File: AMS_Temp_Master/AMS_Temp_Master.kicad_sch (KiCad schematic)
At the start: 9 parts, among them J1 Conn_01x06_Pin, J2 Conn_01x02_Pin, J3 Conn_01x04_Pin, J4 Conn_01x04_Pin, U1 ATmega328P-A, U2 MCP2515-xSO, U3 MCP2551-I-SN, U4 LD1117S50TR_SOT223, Y1 CSTCE16M0V53-R0

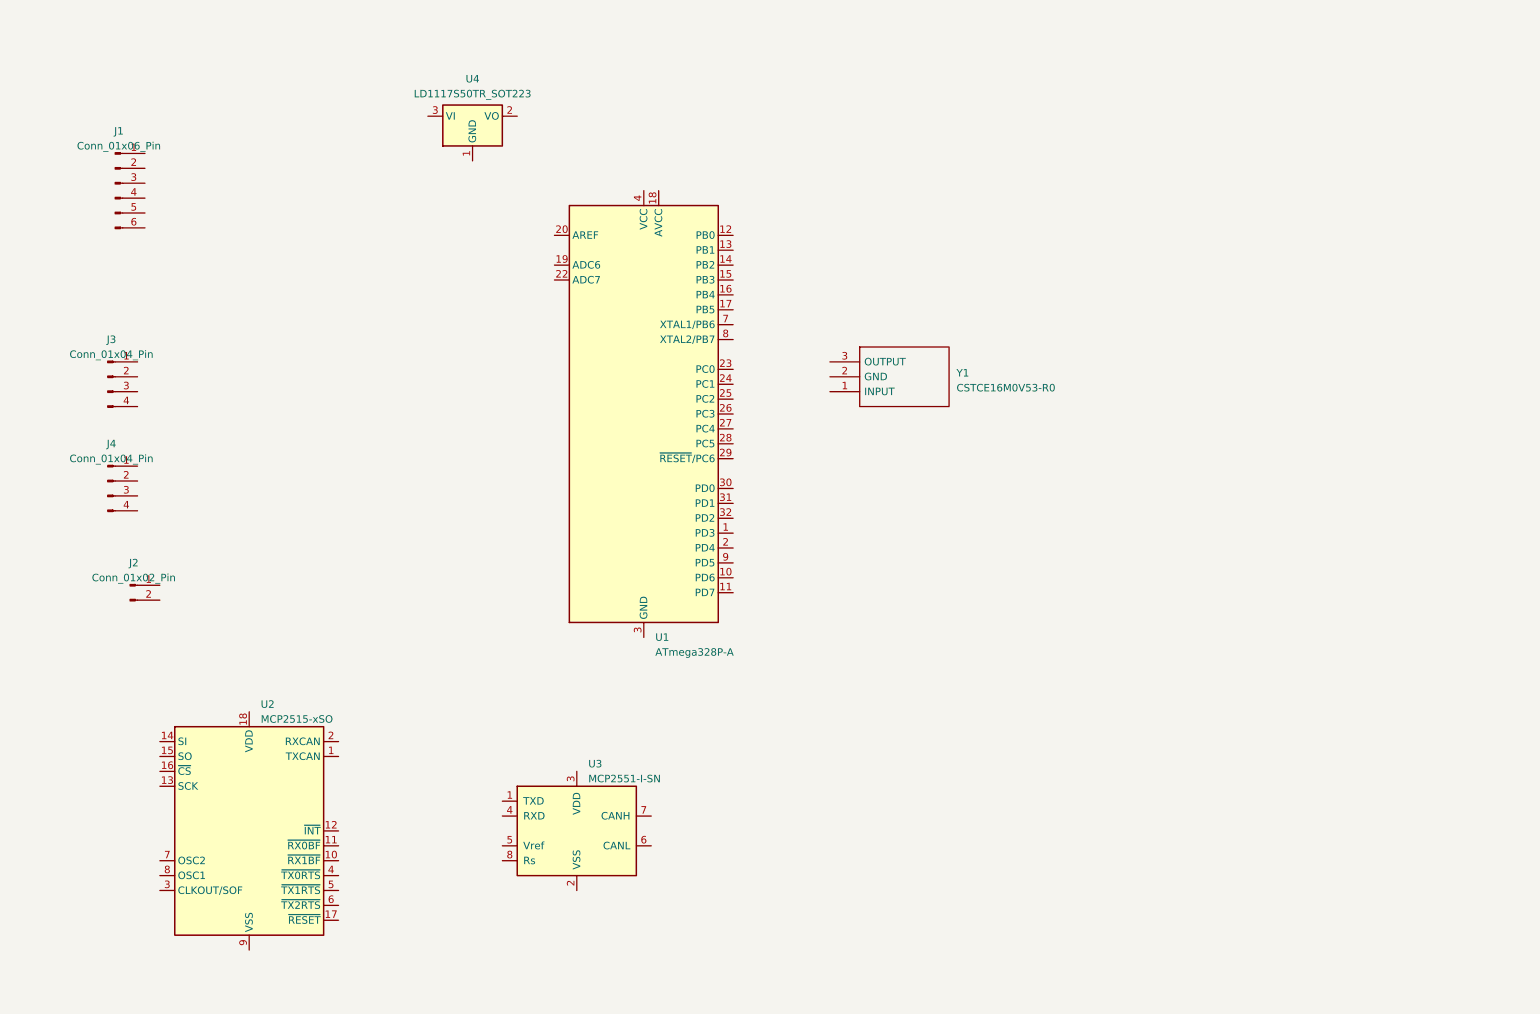
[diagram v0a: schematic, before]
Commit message: Complete AMS_Temp_Master Circuit Schematics and modify
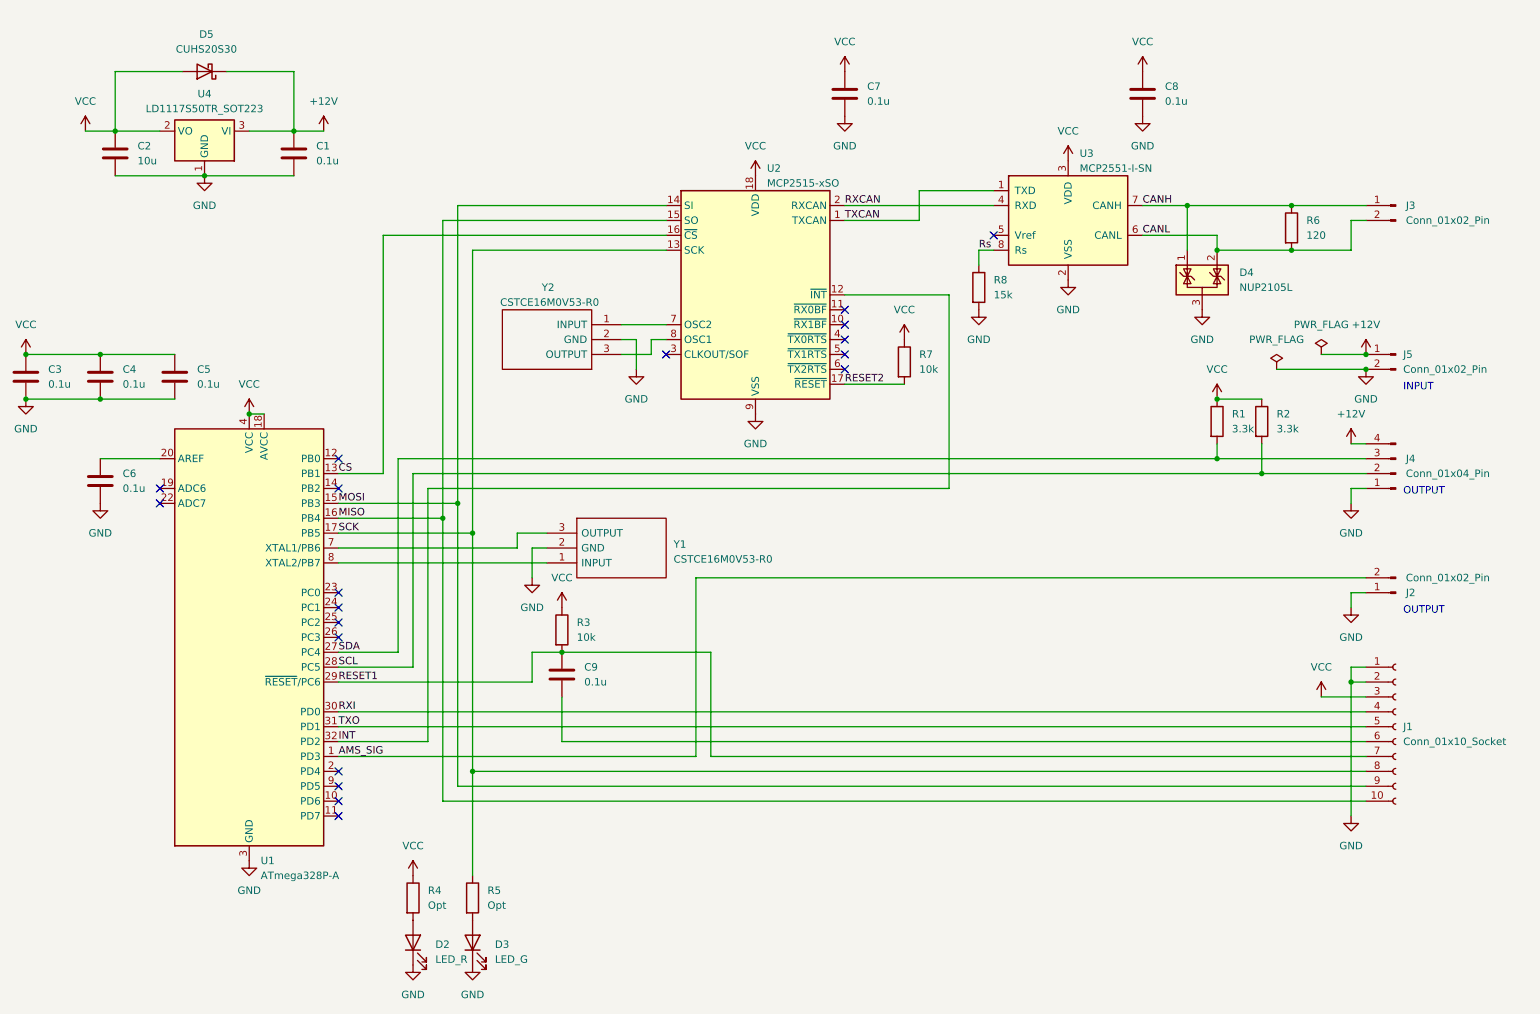
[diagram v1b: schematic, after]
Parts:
- removed J1: Conn_01x06_Pin, symbol Connector:Conn_01x06_Pin
- removed J3: Conn_01x04_Pin, symbol Connector:Conn_01x04_Pin
- added C1, C3, C4, C5, C6, C7, C8, C9: 0.1u, Capacitor_SMD:C_0603_1608Metric, symbol Device:C
- added C2: 10u, Capacitor_SMD:C_0603_1608Metric, symbol Device:C
- added D2: LED_R, LED_SMD:LED_0603_1608Metric, symbol Device:LED
- added D3: LED_G, LED_SMD:LED_0603_1608Metric, symbol Device:LED
- added D4: NUP2105L, Package_TO_SOT_SMD:SOT-23, symbol Power_Protection:NUP2105L
- added D5: CUHS20S30, SamacSys_Parts:CUHS20S40H3F, symbol Device:D_Schottky
- added J1: Conn_01x10_Socket, Connector_PinSocket_2.54mm:PinSocket_1x10_P2.54mm_Vertical, symbol Connector:Conn_01x10_Socket
- added J3, J5: Conn_01x02_Pin, Connector_JST:JST_XH_S2B-XH-A_1x02_P2.50mm_Horizontal, symbol Connector:Conn_01x02_Pin
- added R1, R2: 3.3k, Resistor_SMD:R_0603_1608Metric, symbol Device:R
- added R3, R7: 10k, Resistor_SMD:R_0603_1608Metric, symbol Device:R
- added R4, R5: Opt, Resistor_SMD:R_0603_1608Metric, symbol Device:R
- added R6: 120, Resistor_SMD:R_0603_1608Metric, symbol Device:R
- added R8: 15k, Resistor_SMD:R_0603_1608Metric, symbol Device:R
- added Y2: CSTCE16M0V53-R0, CSTCE16M0V53R0, symbol SamacSys_Parts:CSTCE16M0V53-R0
- J2: footprint (none) -> Connector_JST:JST_XH_S2B-XH-A_1x02_P2.50mm_Horizontal
- J4: footprint (none) -> Connector_JST:JST_XH_S4B-XH-A_1x04_P2.50mm_Horizontal
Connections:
- net AMS_SIG: now reaches U1.1 (PD3)
- net AMS_SIG: now also J2.2 (Pin_2)
- net CS: now reaches U1.13 (PB1)
- net CS: now also U2.16 (~{CS})
- net MOSI: now reaches U1.15 (PB3)
- net MOSI: now also U2.14 (SI), J1.9 (Pin_9)
- net MISO: now reaches U1.16 (PB4)
- net MISO: now also U2.15 (SO), J1.10 (Pin_10)
- net SCK: now reaches U1.17 (PB5)
- net SCK: now also U2.13 (SCK), J1.8 (Pin_8), R5.1
- net VCC: now reaches U1.18 (AVCC)
- net VCC: now also U1.4 (VCC), U1.6 (VCC), U2.18 (VDD), U3.3 (VDD), U4.2 (VO), C2.1, C3.1, C4.1, C5.1, C7.1, C8.1, D5.2 (A), J1.3 (Pin_3), R1.1, R2.1, R3.1, R4.1, R7.1
- net at U1.20 (AREF): now also C6.1
- net GND: now reaches U1.21 (GND), U1.3 (GND), U1.5 (GND)
- net GND: now also J2.1 (Pin_1), J4.1 (Pin_1), U2.9 (VSS), U3.2 (VSS), U4.1 (GND), Y1.2 (GND), C1.2, C2.2, C3.2, C4.2, C5.2, C6.2, C7.2, C8.2, D2.1 (K), D3.1 (K), D4.3 (A), J1.1 (Pin_1), J1.2 (Pin_2), J5.2 (Pin_2), R8.2, Y2.2 (GND)
- net SDA: now reaches U1.27 (PC4)
- net SDA: now also J4.3 (Pin_3), R1.2
- net SCL: now reaches U1.28 (PC5)
- net SCL: now also J4.2 (Pin_2), R2.2
- net RESET1: now reaches U1.29 (~{RESET}/PC6)
- net RESET1: now also C9.1, J1.7 (Pin_7), R3.2
- net RXI: now reaches U1.30 (PD0)
- net RXI: now also J1.4 (Pin_4)
- net TXO: now reaches U1.31 (PD1)
- net TXO: now also J1.5 (Pin_5)
- net INT: now reaches U1.32 (PD2)
- net INT: now also U2.12 (~{INT})
- net at U1.7 (XTAL1/PB6): now also Y1.3 (OUTPUT)
- net at U1.8 (XTAL2/PB7): now also Y1.1 (INPUT)
- net +12V: now reaches J4.4 (Pin_4)
- net +12V: now also U4.3 (VI), C1.1, D5.1 (K), J5.1 (Pin_1)
- net TXCAN: now reaches U2.1 (TXCAN)
- net TXCAN: now also U3.1 (TXD)
- net RESET2: now reaches U2.17 (~{RESET})
- net RESET2: now also R7.2
- net RXCAN: now reaches U2.2 (RXCAN)
- net RXCAN: now also U3.4 (RXD)
- net at U2.7 (OSC2): now also Y2.1 (INPUT)
- net at U2.8 (OSC1): now also Y2.3 (OUTPUT)
- net CANL: now reaches U3.6 (CANL)
- net CANL: now also D4.2 (K), J3.2 (Pin_2), R6.2
- net CANH: now reaches U3.7 (CANH)
- net CANH: now also D4.1 (K), J3.1 (Pin_1), R6.1
- net Rs: now reaches U3.8 (Rs)
- net Rs: now also R8.1
- new net: C9.2, J1.6 (Pin_6)
- new net: D3.2 (A), R5.2
- new net: D2.2 (A), R4.2
- no-connect marks 0 -> 19
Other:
- note added: "INPUT"
- note added: "OUTPUT"
- moved on the sheet: J2, J4, U1, U2, U3, U4, Y1

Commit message: 回路図修正, パターン作成
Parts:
- added C10: 470u, Capacitor_SMD:CP_Elec_6.3x5.4_Nichicon, symbol Device:C_Polarized
- added D1: UDZV5.1B, Diode_SMD:D_SOD-323_HandSoldering, symbol Device:D_Zener
- added Q1: AO3401A, Package_TO_SOT_SMD:SOT-23, symbol Transistor_FET:AO3401A
- added R10, R9: 10k, Resistor_SMD:R_0603_1608Metric, symbol Device:R
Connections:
- net +12V: now also C10.1, D1.1 (K), Q1.2 (S); no longer J5.1 (Pin_1)
- net AMS_SIG: now also R10.1
- net GND: now also C10.2, R10.2, R9.2
- net DTR: now reaches C9.2, J1.6 (Pin_6)
- net AREF: now reaches C6.1, U1.20 (AREF)
- net XTAL1: now reaches U1.7 (XTAL1/PB6), Y1.3 (OUTPUT)
- net XTAL2: now reaches U1.8 (XTAL2/PB7), Y1.1 (INPUT)
- new net: D1.2 (A), Q1.1 (G), R9.1
- new net +12Vin: J5.1 (Pin_1), Q1.3 (D)
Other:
- moved on the sheet: C8, D4, J3, J5, R6, R8, U3
